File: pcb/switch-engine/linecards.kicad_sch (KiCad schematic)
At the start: 23 parts, among them J14 ARF6-08-S-D-A-K-TR, J15 ARF6-08-S-D-A-K-TR, J16 CONN_01X10, J17 ARF6-08-S-D-A-K-TR, J18 ARF6-08-S-D-A-K-TR, J19 CONN_01X10, U15 SIT9121AI-2BF-XXS156.250000G, U18 74LVC1T45, U19 74LVC1T45, U20 74LVC1T45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

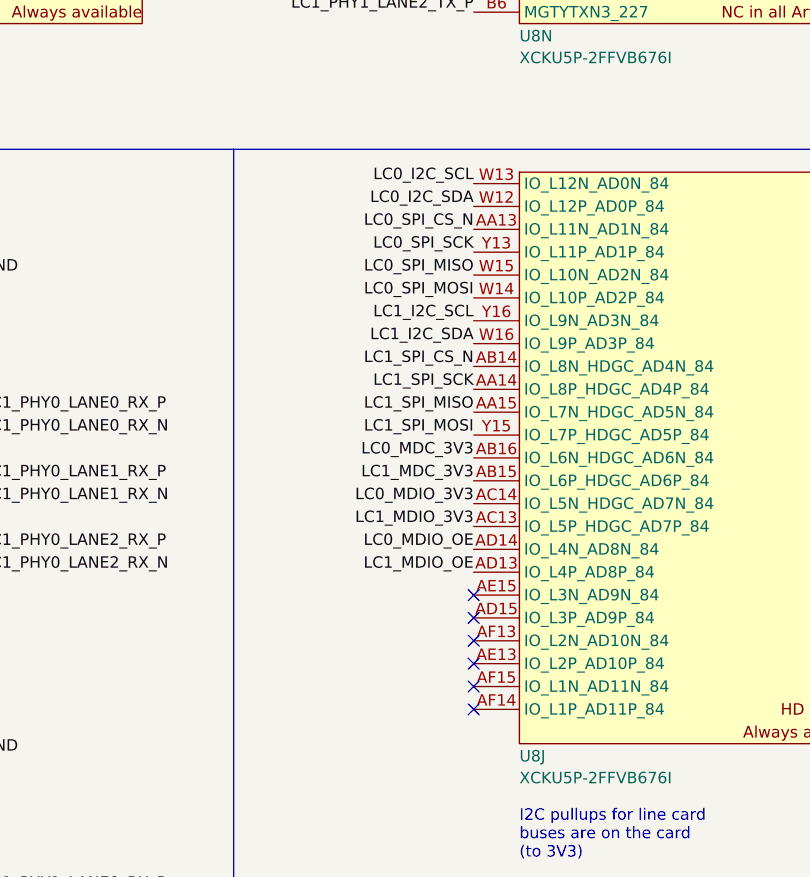
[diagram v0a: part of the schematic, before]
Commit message: Continued routing main MCU and FPGA support parts, hooked up part of boot flash
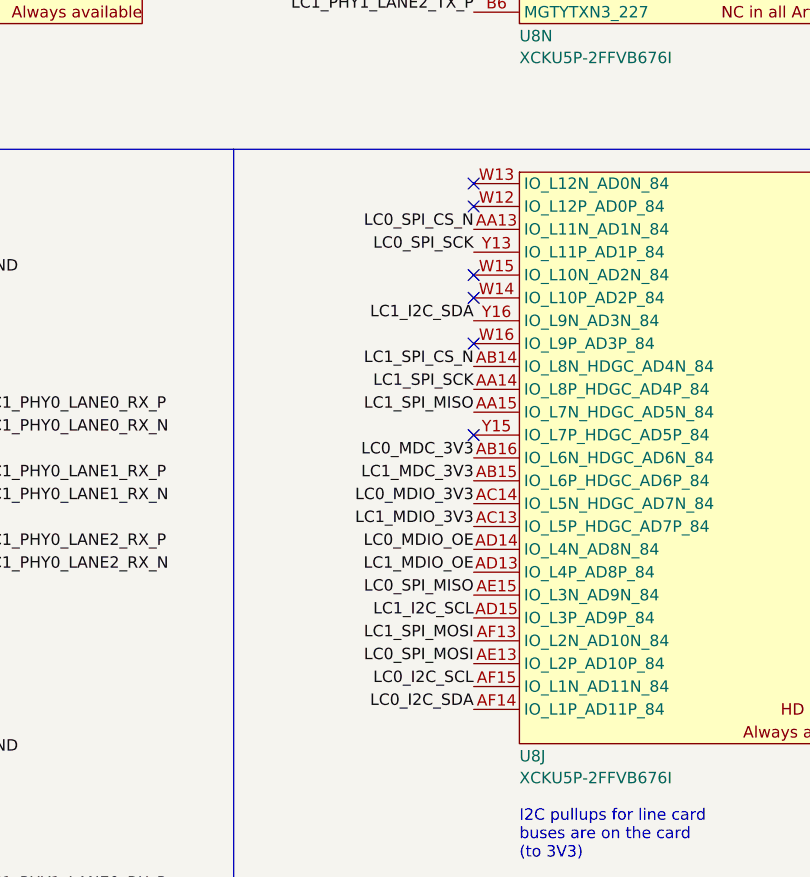
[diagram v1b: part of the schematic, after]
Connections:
- net LC0_I2C_SCL: now also U8.AF15 (IO_L1N_AD11N_84); no longer U8.W13 (IO_L12N_AD0N_84)
- net LC0_I2C_SDA: now also U8.AF14 (IO_L1P_AD11P_84); no longer U8.W12 (IO_L12P_AD0P_84)
- net LC0_SPI_MISO: now also U8.AE15 (IO_L3N_AD9N_84); no longer U8.W15 (IO_L10N_AD2N_84)
- net LC0_SPI_MOSI: now also U8.AE13 (IO_L2P_AD10P_84); no longer U8.W14 (IO_L10P_AD2P_84)
- net LC1_I2C_SCL: now also U8.AD15 (IO_L3P_AD9P_84); no longer U8.Y16 (IO_L9N_AD3N_84)
- net LC1_I2C_SDA: now also U8.Y16 (IO_L9N_AD3N_84); no longer U8.W16 (IO_L9P_AD3P_84)
- net LC1_SPI_MOSI: now also U8.AF13 (IO_L2N_AD10N_84); no longer U8.Y15 (IO_L7P_HDGC_AD5P_84)
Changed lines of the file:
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@@
 	(title_block
 		(title "LATENTRED Ethernet Switch - Main Board")
-		(date "2025-06-06")
+		(date "2025-06-07")
 		(rev "0.1")
 		(company "Antikernel Labs")
@@
 	)
 	(no_connect
-		(at 201.93 187.96)
-	)
-	(no_connect
-		(at 201.93 195.58)
-	)
-	(no_connect
 		(at 39.37 52.07)
 	)
@@
 	)
 	(no_connect
-		(at 201.93 185.42)
-	)
-	(no_connect
 		(at 147.32 241.3)
 	)
 	(no_connect
+		(at 201.93 167.64)
+	)
+	(no_connect
 		(at 64.77 190.5)
 	)
@@
 	)
 	(no_connect
-		(at 201.93 190.5)
-	)
-	(no_connect
 		(at 121.92 243.84)
 	)
 	(no_connect
+		(at 201.93 152.4)
+	)
+	(no_connect
+		(at 201.93 149.86)
+	)
+	(no_connect
 		(at 201.93 44.45)
 	)
@@
 	)
 	(no_connect
+		(at 201.93 142.24)
+	)
+	(no_connect
 		(at 147.32 190.5)
 	)
 	(no_connect
-		(at 201.93 193.04)
-	)
-	(no_connect
 		(at 120.65 49.53)
 	)
@@
 	)
 	(no_connect
+		(at 201.93 157.48)
+	)
+	(no_connect
 		(at 121.92 190.5)
 	)
 	(no_connect
-		(at 201.93 198.12)
-	)
-	(no_connect
 		(at 64.77 243.84)
 	)
@@
 	(no_connect
 		(at 39.37 241.3)
+	)
+	(no_connect
+		(at 201.93 139.7)
 	)
 	(wire
@@
 	)
 	(label "LC0_I2C_SCL"
-		(at 201.93 139.7 180)
+		(at 201.93 195.58 180)
 		(fields_autoplaced yes)
 		(effects
@@
 	)
 	(label "LC1_SPI_MOSI"
-		(at 201.93 167.64 180)
+		(at 201.93 190.5 180)
 		(fields_autoplaced yes)
 		(effects
@@
 	)
 	(label "LC0_SPI_MISO"
-		(at 201.93 149.86 180)
+		(at 201.93 185.42 180)
 		(fields_autoplaced yes)
 		(effects
@@
 	)
 	(label "LC0_I2C_SDA"
-		(at 201.93 142.24 180)
+		(at 201.93 198.12 180)
 		(fields_autoplaced yes)
 		(effects
@@
 	)
 	(label "LC1_I2C_SDA"
-		(at 201.93 157.48 180)
+		(at 201.93 154.94 180)
 		(fields_autoplaced yes)
 		(effects
@@
 	)
 	(label "LC1_I2C_SCL"
-		(at 201.93 154.94 180)
+		(at 201.93 187.96 180)
 		(fields_autoplaced yes)
 		(effects
@@
 	)
 	(label "LC0_SPI_MOSI"
-		(at 201.93 152.4 180)
-		(fields_autoplaced yes)
-		(effects
+		(at 201.93 193.04 180)
+		(fields_autoplaced yes)
+		(effects

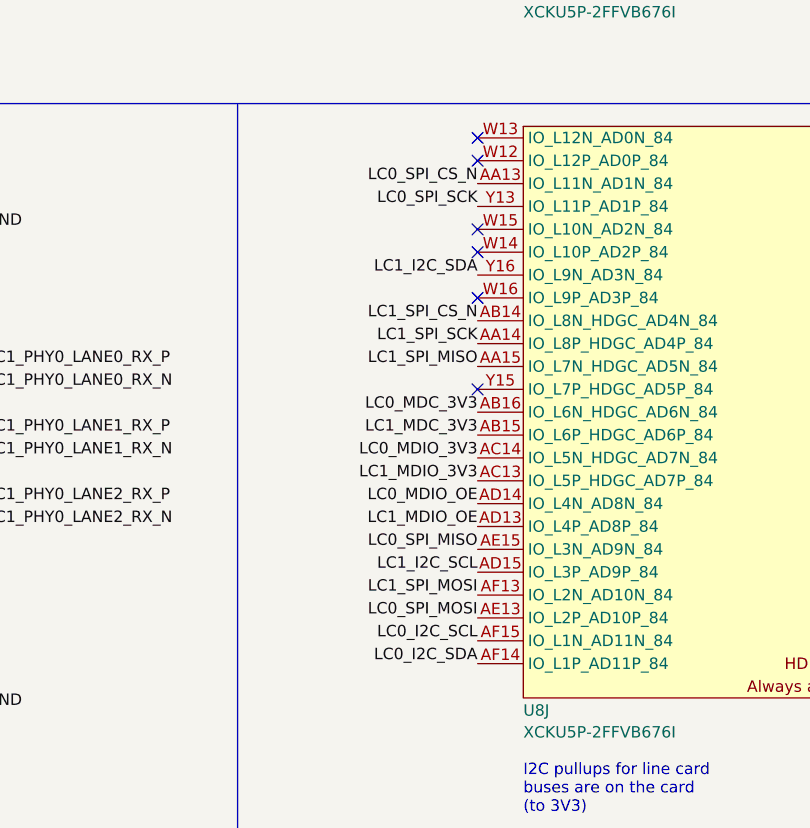
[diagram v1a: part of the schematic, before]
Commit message: Routed line card management low-speed signals
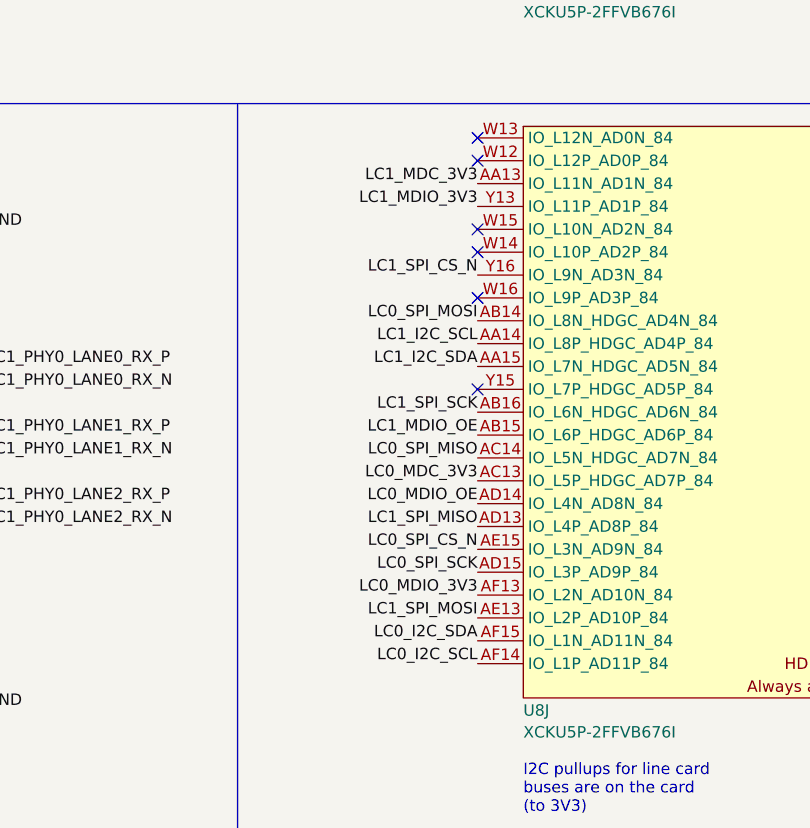
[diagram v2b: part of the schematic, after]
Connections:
- net LC0_I2C_SCL: now also U8.AF14 (IO_L1P_AD11P_84); no longer U8.AF15 (IO_L1N_AD11N_84)
- net LC0_I2C_SDA: now also U8.AF15 (IO_L1N_AD11N_84); no longer U8.AF14 (IO_L1P_AD11P_84)
- net LC0_MDC_3V3: now also U8.AC13 (IO_L5P_HDGC_AD7P_84); no longer U8.AB16 (IO_L6N_HDGC_AD6N_84)
- net LC0_MDIO_3V3: now also U8.AF13 (IO_L2N_AD10N_84); no longer U8.AC14 (IO_L5N_HDGC_AD7N_84)
- net LC0_SPI_CS_N: now also U8.AE15 (IO_L3N_AD9N_84); no longer U8.AA13 (IO_L11N_AD1N_84)
- net LC0_SPI_MISO: now also U8.AC14 (IO_L5N_HDGC_AD7N_84); no longer U8.AE15 (IO_L3N_AD9N_84)
- net LC0_SPI_MOSI: now also U8.AB14 (IO_L8N_HDGC_AD4N_84); no longer U8.AE13 (IO_L2P_AD10P_84)
- net LC0_SPI_SCK: now also U8.AD15 (IO_L3P_AD9P_84); no longer U8.Y13 (IO_L11P_AD1P_84)
- net LC1_I2C_SCL: now also U8.AA14 (IO_L8P_HDGC_AD4P_84); no longer U8.AD15 (IO_L3P_AD9P_84)
- net LC1_I2C_SDA: now also U8.AA15 (IO_L7N_HDGC_AD5N_84); no longer U8.Y16 (IO_L9N_AD3N_84)
- net LC1_MDC_3V3: now also U8.AA13 (IO_L11N_AD1N_84); no longer U8.AB15 (IO_L6P_HDGC_AD6P_84)
- net LC1_MDIO_3V3: now also U8.Y13 (IO_L11P_AD1P_84); no longer U8.AC13 (IO_L5P_HDGC_AD7P_84)
- net LC1_MDIO_OE: now also U8.AB15 (IO_L6P_HDGC_AD6P_84); no longer U8.AD13 (IO_L4P_AD8P_84)
- net LC1_SPI_CS_N: now also U8.Y16 (IO_L9N_AD3N_84); no longer U8.AB14 (IO_L8N_HDGC_AD4N_84)
- net LC1_SPI_MISO: now also U8.AD13 (IO_L4P_AD8P_84); no longer U8.AA15 (IO_L7N_HDGC_AD5N_84)
- net LC1_SPI_MOSI: now also U8.AE13 (IO_L2P_AD10P_84); no longer U8.AF13 (IO_L2N_AD10N_84)
- net LC1_SPI_SCK: now also U8.AB16 (IO_L6N_HDGC_AD6N_84); no longer U8.AA14 (IO_L8P_HDGC_AD4P_84)
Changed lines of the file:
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@@
 	(title_block
 		(title "LATENTRED Ethernet Switch - Main Board")
-		(date "2025-06-07")
+		(date "2025-06-11")
 		(rev "0.1")
 		(company "Antikernel Labs")
@@
 	)
 	(label "LC0_MDIO_3V3"
-		(at 201.93 175.26 180)
+		(at 201.93 190.5 180)
 		(fields_autoplaced yes)
 		(effects
@@
 	)
 	(label "LC0_SPI_CS_N"
-		(at 201.93 144.78 180)
+		(at 201.93 185.42 180)
 		(fields_autoplaced yes)
 		(effects
@@
 	)
 	(label "LC1_MDIO_OE"
-		(at 201.93 182.88 180)
+		(at 201.93 172.72 180)
 		(fields_autoplaced yes)
 		(effects
@@
 	)
 	(label "LC0_I2C_SCL"
-		(at 201.93 195.58 180)
+		(at 201.93 198.12 180)
 		(fields_autoplaced yes)
 		(effects
@@
 	)
 	(label "LC1_SPI_MOSI"
-		(at 201.93 190.5 180)
+		(at 201.93 193.04 180)
 		(fields_autoplaced yes)
 		(effects
@@
 	)
 	(label "LC0_SPI_MISO"
-		(at 201.93 185.42 180)
+		(at 201.93 175.26 180)
 		(fields_autoplaced yes)
 		(effects
@@
 	)
 	(label "LC1_SPI_SCK"
-		(at 201.93 162.56 180)
+		(at 201.93 170.18 180)
 		(fields_autoplaced yes)
 		(effects
@@
 	)
 	(label "LC0_I2C_SDA"
-		(at 201.93 198.12 180)
+		(at 201.93 195.58 180)
 		(fields_autoplaced yes)
 		(effects
@@
 	)
 	(label "LC1_I2C_SDA"
-		(at 201.93 154.94 180)
+		(at 201.93 165.1 180)
 		(fields_autoplaced yes)
 		(effects
@@
 	)
 	(label "LC1_MDC_3V3"
-		(at 201.93 172.72 180)
+		(at 201.93 144.78 180)
 		(fields_autoplaced yes)
 		(effects
@@
 	)
 	(label "LC1_SPI_MISO"
-		(at 201.93 165.1 180)
+		(at 201.93 182.88 180)
 		(fields_autoplaced yes)
 		(effects
@@
 	)
 	(label "LC1_I2C_SCL"
-		(at 201.93 187.96 180)
+		(at 201.93 162.56 180)
 		(fields_autoplaced yes)
 		(effects
@@
 	)
 	(label "LC1_MDIO_3V3"
-		(at 201.93 177.8 180)
+		(at 201.93 147.32 180)
 		(fields_autoplaced yes)
 		(effects
@@
 	)
 	(label "LC0_SPI_MOSI"
-		(at 201.93 193.04 180)
+		(at 201.93 160.02 180)
 		(fields_autoplaced yes)
 		(effects
@@
 	)
 	(label "LC1_SPI_CS_N"
-		(at 201.93 160.02 180)
+		(at 201.93 154.94 180)
 		(fields_autoplaced yes)
 		(effects
@@
 	)
 	(label "LC0_MDC_3V3"
-		(at 201.93 170.18 180)
+		(at 201.93 177.8 180)
 		(fields_autoplaced yes)
 		(effects
@@
 	)
 	(label "LC0_SPI_SCK"
-		(at 201.93 147.32 180)
-		(fields_autoplaced yes)
-		(effects
+		(at 201.93 187.96 180)
+		(fields_autoplaced yes)
+		(effects
